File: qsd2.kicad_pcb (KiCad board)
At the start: 2 copper layers, 100 x 75 mm, 65 parts, among them J1 5-1814832-1, J2 5-1814832-1, J3 Conn_02x08_Odd_Even, J4 SJ-3524-SMT, U1 SN74LVC1G14DBV, U10 GALI-39, U2 SN74LVC1G14DBV, U3 SN74CBT3253, U4 SN74AC74PW, U5 AD8226ARZ-R7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

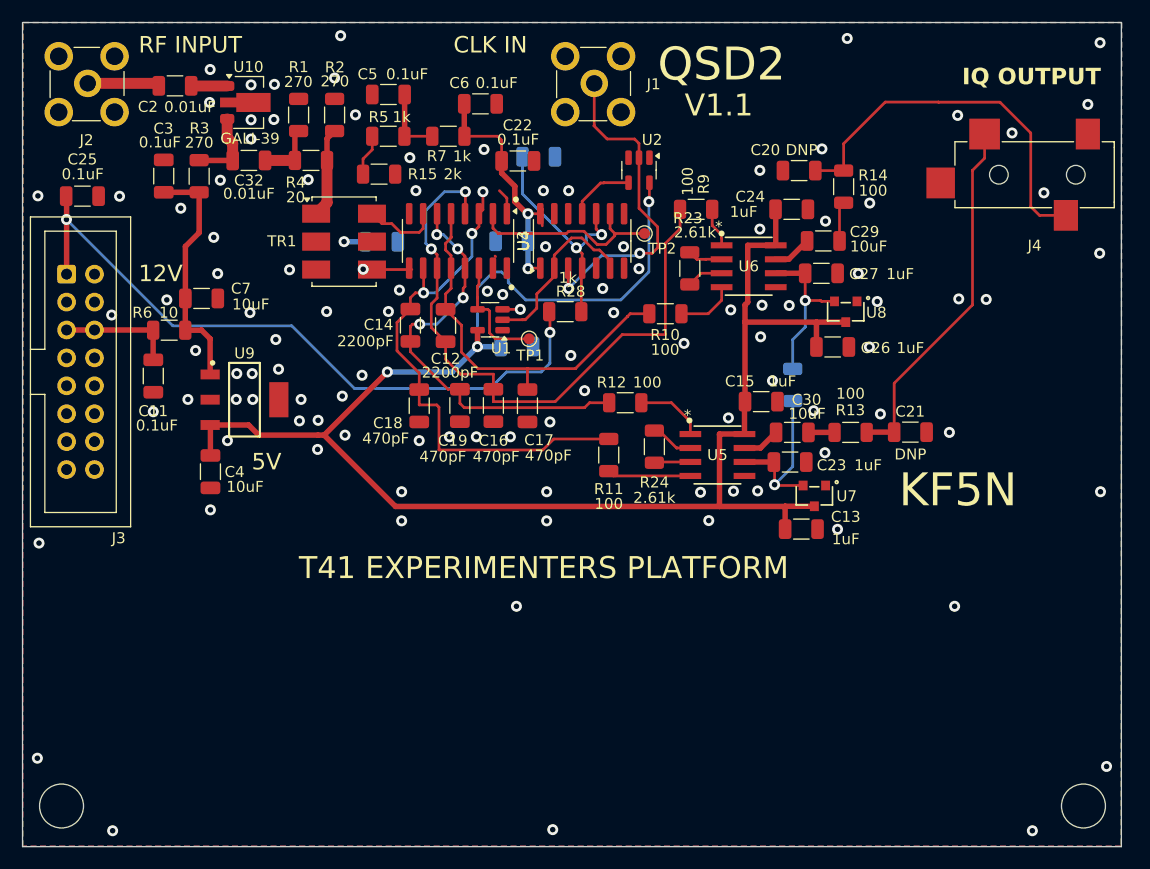
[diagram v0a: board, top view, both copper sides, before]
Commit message: QSD2EZ to V1.0 fab.
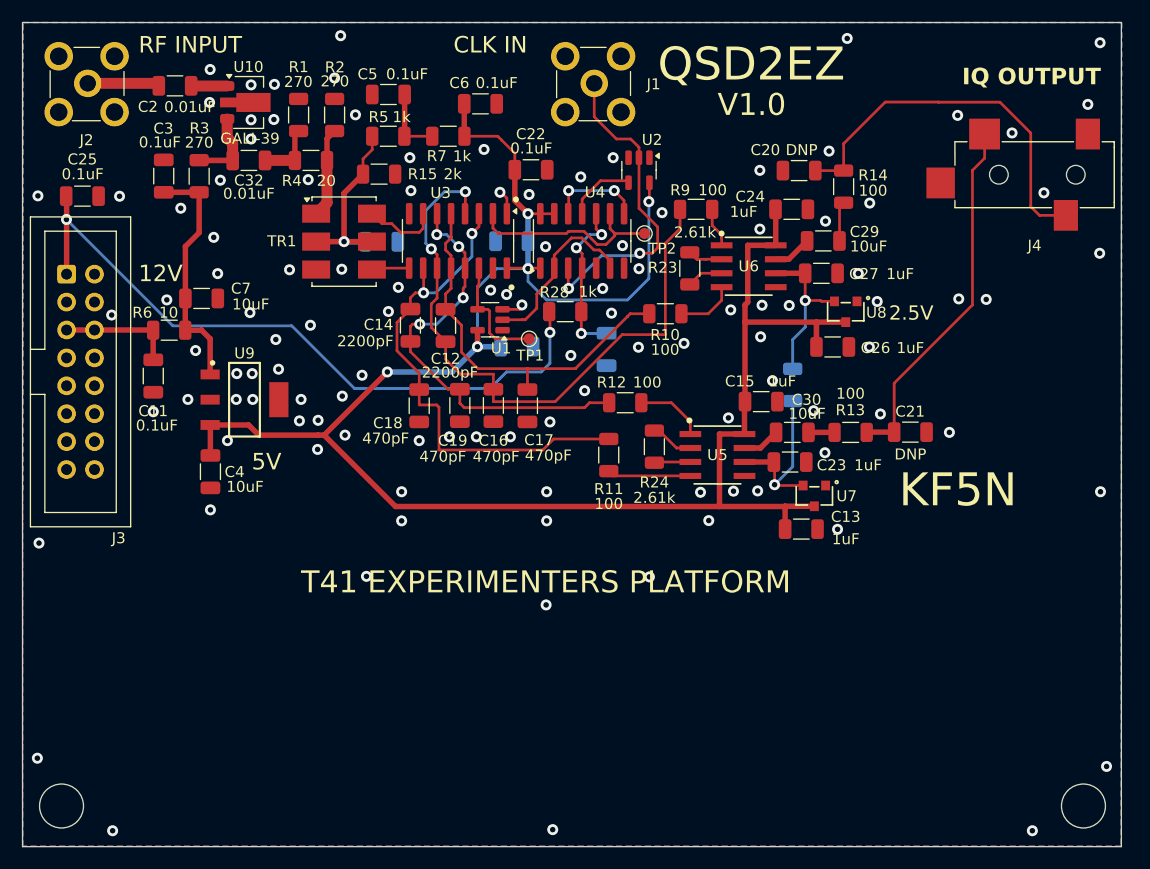
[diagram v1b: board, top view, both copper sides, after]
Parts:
- moved C31 18.6 mm to (152.3, 69.3), turned to 90 degrees
- moved C22 1.45 mm to (145.5, 53.0)
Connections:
- TR1 pad 2: (no net) -> Net-(C33-Pad2)
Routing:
- net Net-(C33-Pad2): track 5.74 -> 17.7 mm
- net /FB2: track 0.00 -> 8.74 mm
- net /PREN: track 21.0 -> 15.3 mm, vias 2 -> 3
- net /5V_FILT: track 182.3 -> 185.1 mm
- net Net-(U3-1B4): track 48.9 -> 46.7 mm, vias 3 -> 2
- net /CLK1: track 30.4 -> 29.6 mm
- net GND: track 4.17 -> 4.62 mm, vias 107 -> 114
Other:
- board text added: "2.5V"
- board text added: "QSD2EZ"
- board text added: "V1.0"
- board text removed: "QSD2"
- board text removed: "V1.1"

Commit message: QSD2EZ with lower connector V1.0 to fab.
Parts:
- moved C25 17.7 mm to (104.7, 73.1)
- moved J3 17.7 mm to (103.2, 80.2)
- moved C11 15.0 mm to (111.2, 86.8)
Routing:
- net /12_0V: track 10.6 -> 28.2 mm
- net /SET: track 63.2 -> 64.6 mm
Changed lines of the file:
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@@
 		)
 		(property "Value" "SN74CBT3253"
-			(at 0 5.9 270)
+			(at 0 5.9 -90)
 			(layer "F.Fab")
 			(hide yes)
@@
 	(footprint "Capacitor_SMD:C_1206_3216Metric"
 		(layer "F.Cu")
-		(at 104.65 55.4)
+		(at 104.65 73.125)
 		(descr "Capacitor SMD 1206 (3216 Metric), square (rectangular) end terminal, IPC_7351 nominal, (Body size source: IPC-SM-782 page 76, https://www.pcb-3d.com/wordpress/wp-content/uploads/ipc-sm-782a_amendment_1_and_2.pdf), generated with kicad-footprint-generator")
 		(tags "capacitor")
@@
 	(footprint "Capacitor_SMD:C_1206_3216Metric"
 		(layer "F.Cu")
-		(at 111.1 71.77 -90)
+		(at 111.15 86.775 -90)
 		(descr "Capacitor SMD 1206 (3216 Metric), square (rectangular) end terminal, IPC_7351 nominal, (Body size source: IPC-SM-782 page 76, https://www.pcb-3d.com/wordpress/wp-content/uploads/ipc-sm-782a_amendment_1_and_2.pdf), generated with kicad-footprint-generator")
 		(tags "capacitor")
 		(property "Reference" "C11"
-			(at 3.19 0.01 0)
+			(at -1.475 -2.9 0)
 			(layer "F.SilkS")
 			(effects
@@
 		)
 		(property "Value" "0.1uF"
-			(at 4.5 -0.33 0)
+			(at 0.075 -3.6 0)
 			(layer "F.SilkS")
 			(effects
@@
 	(footprint "Connector_IDC:IDC-Header_2x08_P2.54mm_Vertical"
 		(layer "F.Cu")
-		(at 103.21 62.5)
+		(at 103.21 80.225)
 		(descr "Through hole IDC box header, 2x08, 2.54mm pitch, DIN 41651 / IEC 60603-13, double rows, https://docs.google.com/spreadsheets/d/16SsEcesNF15N3Lb4niX7dcUr-NY5_MFPQhobNuNppn4/edit#gid=0")
 		(tags "Through hole vertical IDC box header THT 2x08 2.54mm double row")
@@
 		(tags "capacitor")
 		(property "Reference" "C31"
-			(at 0 1.85 270)
+			(at 0 1.85 -90)
 			(layer "B.SilkS")
 			(effects
@@
 		)
 		(property "Value" "0.1uF"
-			(at 0 -1.85 270)
+			(at 0 -1.85 -90)
 			(layer "B.SilkS")
 			(effects
@@
 		)
 		(fp_text user "${REFERENCE}"
-			(at 0 0 270)
+			(at 0 0 -90)
 			(layer "B.Fab")
 			(effects
@@
 	)
 	(via
-		(at 108.03 55.41)
+		(at 108.03 73.135)
 		(size 1)
 		(drill 0.5)
@@
 	)
 	(via
-		(at 111.1 75.02)
+		(at 111.4 90)
 		(size 1)
 		(drill 0.5)
@@
 	)
 	(via
-		(at 100.6 55.375)
+		(at 100.6 73.1)
 		(size 1)
 		(drill 0.5)
@@
 	)
 	(via
-		(at 100.7 86.975)
+		(at 100.7 104.7)
 		(size 1)
 		(drill 0.5)
@@
 	)
 	(segment
+		(start 103.2 73.15)
+		(end 103.175 73.125)
+		(width 0.5)
+		(layer "F.Cu")
+		(net 9)
+	)
+	(segment
+		(start 103.21 80.225)
+		(end 103.21 75.26)
+		(width 0.5)
+		(layer "F.Cu")
+		(net 9)
+	)
+	(segment
 		(start 147.2 65.9855)
 		(end 147.1275 65.913)
@@
 	)
 	(segment
-		(start 103.21 57.535)
-		(end 103.2 57.525)
+		(start 103.21 75.26)
+		(end 103.2 75.25)
 		(width 0.5)
 		(layer "F.Cu")
@@
 	)
 	(segment
-		(start 103.21 57.515)
-		(end 103.21 55.435)
+		(start 103.21 75.24)
+		(end 103.21 73.16)
 		(width 0.5)
 		(layer "F.Cu")
@@
 	)
 	(segment
-		(start 103.2 57.525)
-		(end 103.21 57.515)
+		(start 103.2 75.25)
+		(end 103.21 75.24)
 		(width 0.5)
 		(layer "F.Cu")
@@
 	)
 	(segment
-		(start 103.21 62.5)
-		(end 103.21 57.535)
-		(width 0.5)
+		(start 103.21 73.16)
+		(end 103.175 73.125)
+		(width 0.25)
 		(layer "F.Cu")
 		(net 9)
 	)
 	(segment
-		(start 103.21 55.435)
-		(end 103.175 55.4)
-		(width 0.25)
+		(start 103.2 75.25)
+		(end 103.2 73.15)
+		(width 0.5)
 		(layer "F.Cu")
 		(net 9)
@@
 	)
 	(via
-		(at 103.2 57.525)
+		(at 103.2 75.25)
 		(size 1)
 		(drill 0.5)
@@
 	)
 	(segment
-		(start 146.4 71.4)
-		(end 143.25 71.4)
+		(start 143.25 71.4)
+		(end 141.75 72.9)
 		(width 0.25)
 		(layer "B.Cu")
@@
 	)
 	(segment
-		(start 147.15 70.65)
-		(end 146.4 71.4)
+		(start 129.4 72.9)
+		(end 123.7 67.2)
 		(width 0.25)
 		(layer "B.Cu")
@@
 	)
 	(segment
-		(start 112.875 67.2)
-		(end 103.2 57.525)
+		(start 146.4 71.4)
+		(end 143.25 71.4)
 		(width 0.25)
 		(layer "B.Cu")
@@
 	)
 	(segment
-		(start 141.75 72.9)
-		(end 129.4 72.9)
+		(start 111.25 67.2)
+		(end 103.2 75.25)
 		(width 0.25)
 		(layer "B.Cu")
@@
 	)
 	(segment
-		(start 143.25 71.4)
-		(end 141.75 72.9)
-		(width 0.25)
-		(layer "B.Cu")
-		(net 9)
-	)
-	(segment
-		(start 129.4 72.9)
-		(end 123.7 67.2)
+		(start 141.75 72.9)
+		(end 129.4 72.9)
 		(width 0.25)
 		(layer "B.Cu")
@@
 	)
 	(segment
-		(start 123.7 67.2)
-		(end 112.875 67.2)
-		(width 0.25)
-		(layer "B.Cu")
-		(net 9)
-	)
-	(segment
 		(start 147.2 70.6)
-		(end 147.15 70.65)
+		(end 146.4 71.4)
 		(width 0.25)
 		(layer "B.Cu")
@@
 	)
 	(segment
-		(start 103.21 62.5)
-		(end 103.225 62.5)
+		(start 123.7 67.2)
+		(end 111.25 67.2)
 		(width 0.25)
 		(layer "B.Cu")
@@
 	)
 	(segment
-		(start 111.0875 70.2825)
-		(end 111.1 70.295)
+		(start 105.75 85.305)
+		(end 106.155 85.305)
 		(width 0.5)
 		(layer "F.Cu")
@@
 	)
 	(segment
-		(start 105.75 67.58)
-		(end 111.0675 67.58)
+		(start 106.155 85.305)
+		(end 106.16 85.3)
 		(width 0.5)
 		(layer "F.Cu")
@@
 	)
 	(segment
+		(start 106.16 85.3)
+		(end 111.15 85.3)
+		(width 1)
+		(layer "F.Cu")
+		(net 14)
+	)
+	(segment
 		(start 111.0675 67.58)
 		(end 111.0875 67.6)
@@
 	(segment
 		(start 111.0875 67.6)
-		(end 111.0875 70.2825)
-		(width 0.5)
+		(end 111.0875 85.2375)
+		(width 1)
 		(layer "F.Cu")
 		(net 14)
 	)
 	(segment
-		(start 103.21 67.58)
-		(end 105.75 67.58)
+		(start 111.0875 85.2375)
+		(end 111.15 85.3)
 		(width 0.5)
 		(layer "F.Cu")
@@
 	)
 	(segment
+		(start 103.21 85.305)
+		(end 105.75 85.305)
+		(width 1)
+		(layer "F.Cu")
+		(net 14)
+	)
+	(segment
+		(start 103.21 85.305)
+		(end 105.75 85.305)
+		(width 1)
+		(layer "B.Cu")
+		(net 14)
+	)
+	(segment
 		(start 154.55 50.2)
 		(end 153.25 50.2)
@@
 		(polygon
 			(pts
-				(xy 110.19 71.058748) (xy 112.01 71.058748) (xy 112.01 72.481252) (xy 110.19 72.481252)
+				(xy 110.49 86.063748) (xy 112.31 86.063748) (xy 112.31 87.486252) (xy 110.49 87.486252)
 			)
 		)
@@
 		(polygon
 			(pts
-				(xy 103.95 56.3) (xy 103.95 54.5) (xy 105.35 54.5) (xy 105.35 56.3)
+				(xy 103.95 74.025) (xy 103.95 72.225) (xy 105.35 72.225) (xy 105.35 74.025)
 			)
 		)
